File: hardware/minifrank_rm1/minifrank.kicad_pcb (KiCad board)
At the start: 2 copper layers, 66.5 x 48.3 mm, 94 parts, among them Q1 BC850, Q2 BC850, SW1 Flash Button, SW2 Reset Button, U1 NCP1117 3.3, Y1 12 MHz

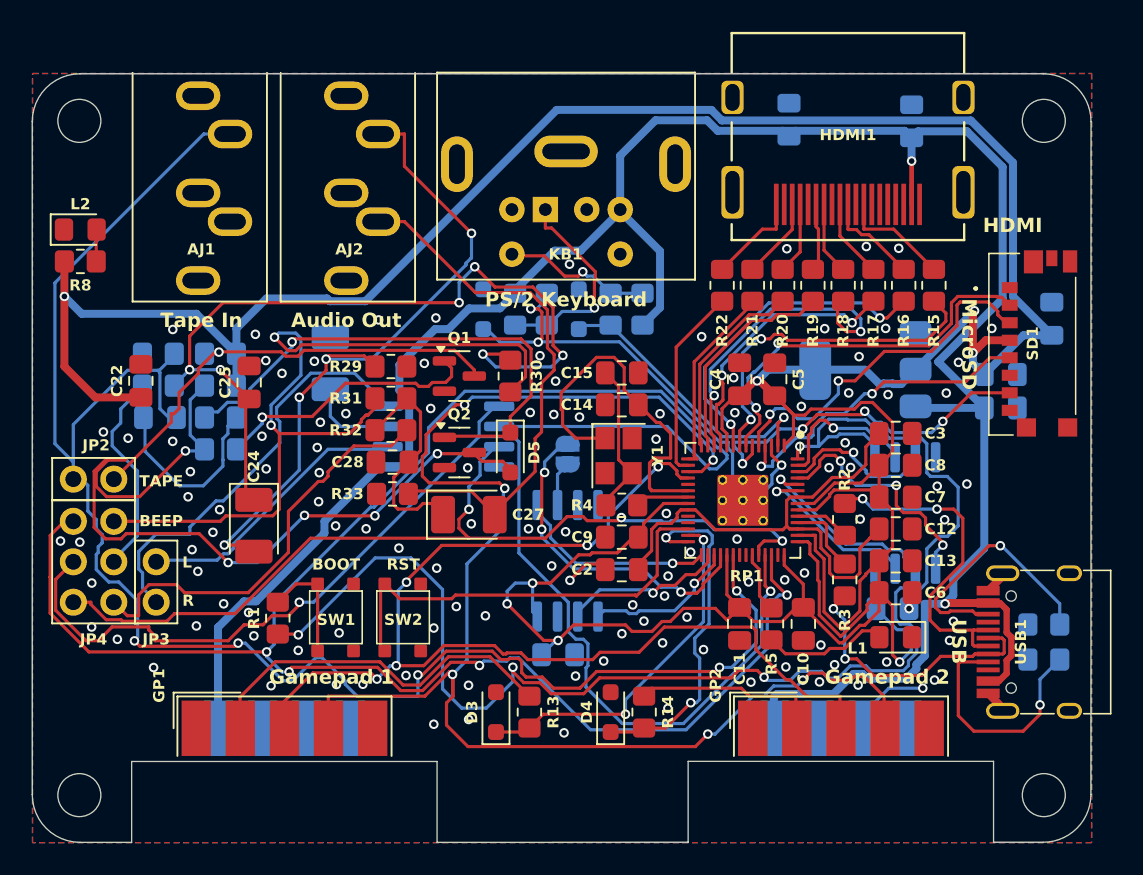
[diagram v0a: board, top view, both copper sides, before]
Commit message: Fixed tape loading bug on all PCBs
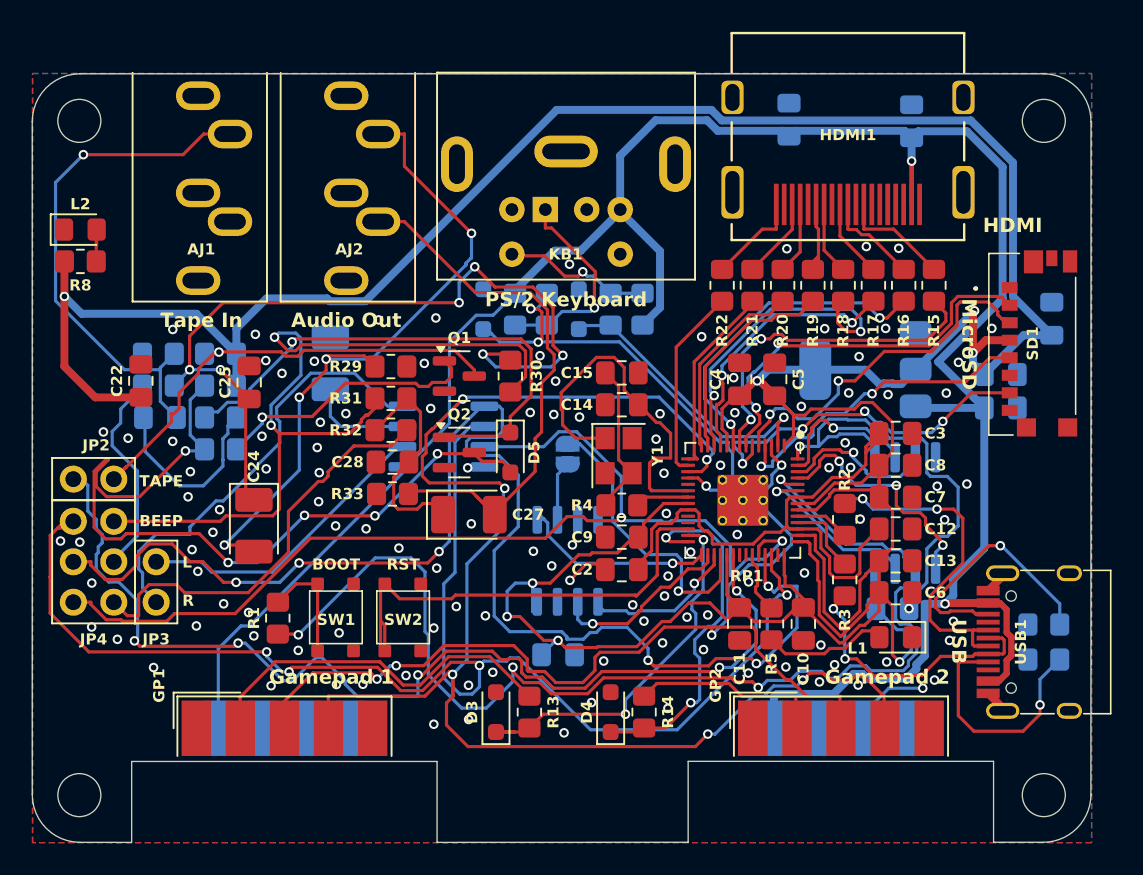
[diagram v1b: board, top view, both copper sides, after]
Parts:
- PSR1, TDA1: footprint FRANK:SOIC-8 -> FRANK:SO-8
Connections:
- AJ1 pad T: /LOAD_IN_D -> Net-(AJ1-PadT)
- C23 pad 1: /LOAD_IN_D -> Net-(AJ1-PadT)
- R27 pad 1: /LOAD_IN_D -> Net-(AJ1-PadT)
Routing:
- net /LOAD_IN_D: track 106.8 -> 66.2 mm
- net /AUDIO_B: track 121.6 -> 88.3 mm
- net Net-(AJ1-PadT): track 0.00 -> 32.8 mm, vias 0 -> 1
- net /AUDIO_R: track 57.8 -> 66.5 mm, vias 3 -> 2
- net /AUDIO_L: track 79.8 -> 85.6 mm, vias 2 -> 6
- net +3V3: track 258.0 -> 263.5 mm
- net /GP_J3: track 71.4 -> 65.9 mm, vias 5 -> 4
- net Net-(C24-Pad1): track 50.1 -> 52.8 mm
- net /RUN: track 27.1 -> 29.7 mm
- net /PSR_SOSIO: track 20.6 -> 18.4 mm, vias 3 -> 1
- net Net-(RP1-VREG_VOUT): track 33.4 -> 35.6 mm
- net /GP_J4: track 92.2 -> 94.2 mm
- net /Audio Out/R: track 33.2 -> 35.1 mm
- net /Audio Out/LEFT_TDA: track 17.5 -> 19.0 mm
- net /PSR_SCLK: track 10.1 -> 11.6 mm
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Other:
- board text added: "HW RM1 2.02"
- board text removed: "HW RM1 2.01"
